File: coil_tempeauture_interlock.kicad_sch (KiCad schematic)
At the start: 41 parts, among them J1 Conn_01x10_Pin, J10 -12V, J11 +12V, J2 Conn_01x10_Pin, J4 Conn_01x05, J6 Output1, J7 Output2, J8 Thermalcouple1, J9 Thermocouple2, Q1 BS107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

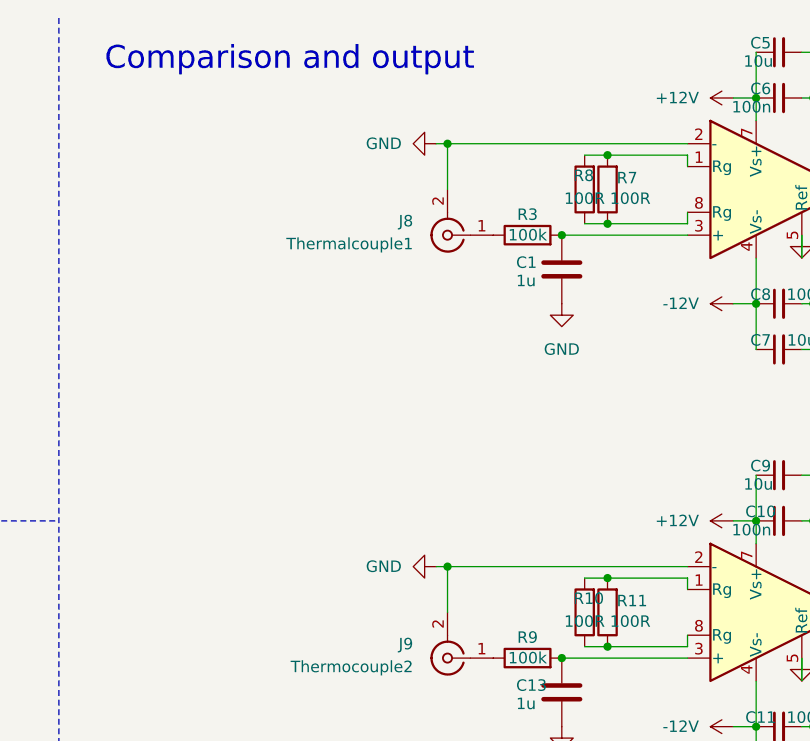
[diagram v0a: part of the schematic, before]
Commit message: isolate thermocouple input
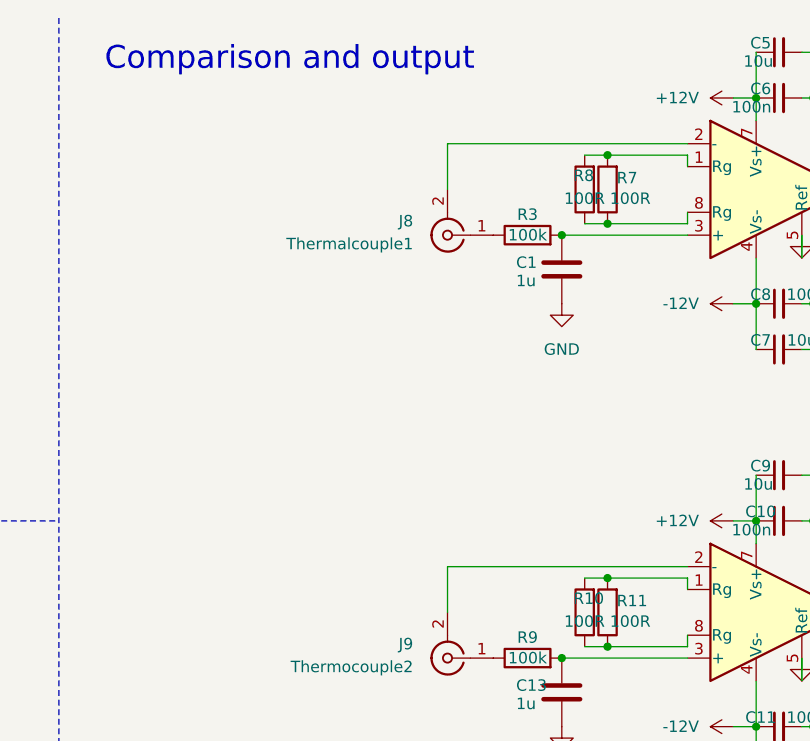
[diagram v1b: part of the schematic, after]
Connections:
- net GND: no longer J8.2 (Ext), J9.2 (Ext), U2.2 (-), U3.2 (-)
- new net: J9.2 (Ext), U3.2 (-)
- new net: J8.2 (Ext), U2.2 (-)
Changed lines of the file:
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@@
 	)
 	(junction
-		(at 109.22 73.66)
-		(diameter 0)
-		(color 0 0 0 0)
-	)
-	(junction
 		(at 149.86 21.59)
 		(diameter 0)
@@
 	)
 	(junction
-		(at 109.22 26.67)
-		(diameter 0)
-		(color 0 0 0 0)
-	)
-	(junction
 		(at 204.47 91.44)
 		(diameter 0)
@@
 	(wire
 		(pts
-			(xy 107.95 26.67) (xy 109.22 26.67)
-		)
-		(stroke
-			(width 0)
-			(type default)
-		)
-	)
-	(wire
-		(pts
 			(xy 151.13 21.59) (xy 149.86 21.59)
 		)
@@
 	(wire
 		(pts
-			(xy 107.95 73.66) (xy 109.22 73.66)
-		)
-		(stroke
-			(width 0)
-			(type default)
-		)
-	)
-	(wire
-		(pts
 			(xy 109.22 73.66) (xy 109.22 78.74)
 		)
@@
 	(symbol
 		(lib_id "power:GND")
-		(at 107.95 26.67 270)
-		(unit 1)
-		(exclude_from_sim no)
-		(in_bom yes)
-		(on_board yes)
-		(dnp no)
-		(fields_autoplaced yes)
-		(property "Reference" "#PWR028"
-			(at 101.6 26.67 0)
-			(effects
-				(font
-					(size 1.27 1.27)
-				)
-				(hide yes)
-			)
-		)
-		(property "Value" "GND"
-			(at 104.14 26.6699 90)
-			(effects
-				(font
-					(size 1.27 1.27)
-				)
-				(justify right)
-			)
-		)
-		(property "Footprint" ""
-			(at 107.95 26.67 0)
-			(effects
-				(font
-					(size 1.27 1.27)
-				)
-				(hide yes)
-			)
-		)
-		(property "Datasheet" ""
-			(at 107.95 26.67 0)
-			(effects
-				(font
-					(size 1.27 1.27)
-				)
-				(hide yes)
-			)
-		)
-		(property "Description" "Power symbol creates a global label with name \"GND\" , ground"
-			(at 107.95 26.67 0)
-			(effects
-				(font
-					(size 1.27 1.27)
-				)
-				(hide yes)
-			)
-		)
-		(pin "1"
-		)
-		(instances
-			(project ""
-				(path "/9c6abd11-1aac-4f08-8b79-cac116854bcb"
-					(reference "#PWR028")
-					(unit 1)
-				)
-			)
-		)
-	)
-	(symbol
-		(lib_id "power:GND")
 		(at 110.49 153.67 0)
 		(unit 1)
@@
 					(unit 1)
 				)
-			)
-		)
-	)
-	(symbol
-		(lib_id "power:GND")
-		(at 107.95 73.66 270)
-		(unit 1)
-		(exclude_from_sim no)
-		(in_bom yes)
-		(on_board yes)
-		(dnp no)
-		(fields_autoplaced yes)
-		(property "Reference" "#PWR045"
-			(at 101.6 73.66 0)
-			(effects
-				(font
-					(size 1.27 1.27)
-				)
-				(hide yes)
-			)
-		)
-		(property "Value" "GND"
-			(at 104.14 73.6599 90)
-			(effects
-				(font
-					(size 1.27 1.27)
-				)
-				(justify right)
-			)
-		)
-		(property "Footprint" ""
-			(at 107.95 73.66 0)
-			(effects
-				(font
-					(size 1.27 1.27)
-				)
-				(hide yes)
-			)
-		)
-		(property "Datasheet" ""
-			(at 107.95 73.66 0)
-			(effects
-				(font
-					(size 1.27 1.27)
-				)
-				(hide yes)
-			)
-		)
-		(property "Description" "Power symbol creates a global label with name \"GND\" , ground"
-			(at 107.95 73.66 0)
-			(effects
-				(font
-					(size 1.27 1.27)
-				)
-				(hide yes)
-			)
-		)
-		(pin "1"
-		)
-		(instances
-			(project "coil_tempeauture_interlock"
-				(path "/9c6abd11-1aac-4f08-8b79-cac116854bcb"
-					(reference "#PWR045")
-					(unit 1)
-				)
